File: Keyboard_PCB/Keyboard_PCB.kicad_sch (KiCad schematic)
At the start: 59 parts, among them J2 Battery, J3 JTAG, J4 EBUS, SW71 BTN, SW72 BTN, U1 STM32H7B0VBTx, U3 AP7343, U4 M95P32, Y1 25MHz, Y2 32.768 KHz

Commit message: Cleaned up project
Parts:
- removed C15, C16: 1u, Capacitor_SMD:C_0603_1608Metric, symbol Device:C_Small
- removed C21, C22: 2u2, Capacitor_SMD:C_0603_1608Metric, symbol Device:C_Small
- removed C27: 100n, Capacitor_SMD:C_0603_1608Metric, symbol Device:C_Small
- removed C9: 4u7, Capacitor_SMD:C_0603_1608Metric, symbol Device:C_Small
- removed D69: BAT54C, Package_TO_SOT_SMD:SOT-23, symbol Diode:BAT54C
- removed D72: CHARGING, LED_SMD:LED_0603_1608Metric, symbol Device:LED
- removed D73: CHARGED, LED_SMD:LED_0603_1608Metric, symbol Device:LED
- removed H1, H2, H3, H4, H5, H6: MountingHole_Pad, MountingHole:MountingHole_2.2mm_M2_DIN965_Pad, symbol Mechanical:MountingHole_Pad
- removed J2: Battery, Connector_PinHeader_2.00mm:PinHeader_1x02_P2.00mm_Vertical, symbol Connector_Generic:Conn_02x01
- removed J4: EBUS, Connector_PinHeader_2.00mm:PinHeader_2x04_P2.00mm_Vertical, symbol Connector_Generic:Conn_02x04_Counter_Clockwise
- removed JP1: Battery_EN, Jumper:SolderJumper-2_P1.3mm_Open_TrianglePad1.0x1.5mm, symbol Jumper:SolderJumper_2_Open
- removed R17: 47, Resistor_SMD:R_0603_1608Metric, symbol Device:R_Small
- removed R22: 2k2, Resistor_SMD:R_0603_1608Metric, symbol Device:R_Small
- removed R23: (1200 / batt_mAh) K ohm, Resistor_SMD:R_0603_1608Metric, symbol Device:R_Small
- removed R24, R25: 1k, Resistor_SMD:R_0603_1608Metric, symbol Device:R_Small
- removed TP1, TP2, TP3, TP4, TP5, TP6: TestPoint, TestPoint:TestPoint_THTPad_D2.0mm_Drill1.0mm, symbol Connector:TestPoint
- removed U1: STM32H7B0VBTx, Package_QFP:LQFP-100_14x14mm_P0.5mm, symbol MCU_ST_STM32H7:STM32H7B0VBTx
- removed U3: AP7343, Custom:SOT-25, symbol Marijn:AP7343
- removed U4: M95P32, Package_SO:PowerIntegrations_SO-8, symbol Marijn:M95P32
- removed U6: ~, Package_SO:MSOP-8_3x3mm_P0.65mm, symbol Marijn:TP4056
- added U1: STM32F412CGUx, Package_DFN_QFN:QFN-48-1EP_7x7mm_P0.5mm_EP5.6x5.6mm, symbol MCU_ST_STM32F4:STM32F412CGUx
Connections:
- new net: U1.23 (VSS), U1.35 (VSS), U1.47 (VSS), U1.49 (VSS)
- no-connect marks 30 -> 0
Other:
- removed sheet Grid
- removed sheet LCD
- note added: "STM32F412"
- note removed: "Battery Charging"
- note removed: "EEPROM"
- note removed: "Expansion BUS: 1. connection detection pin 1p 2. power 2p 3. tx only uart for keypresses 1p 4. SPI bus 4p TODO: bus takes up almost whole width of pcb topside"
- note removed: "IO"
- note removed: "LCD"
- note removed: "Mounting"
- note removed: "STM32H7B0vbt6"
- note removed: "VBAT"
- moved on the sheet: C1, C2, C28, C3, C4, C5, C6, C7, D70, D71, J3, L1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

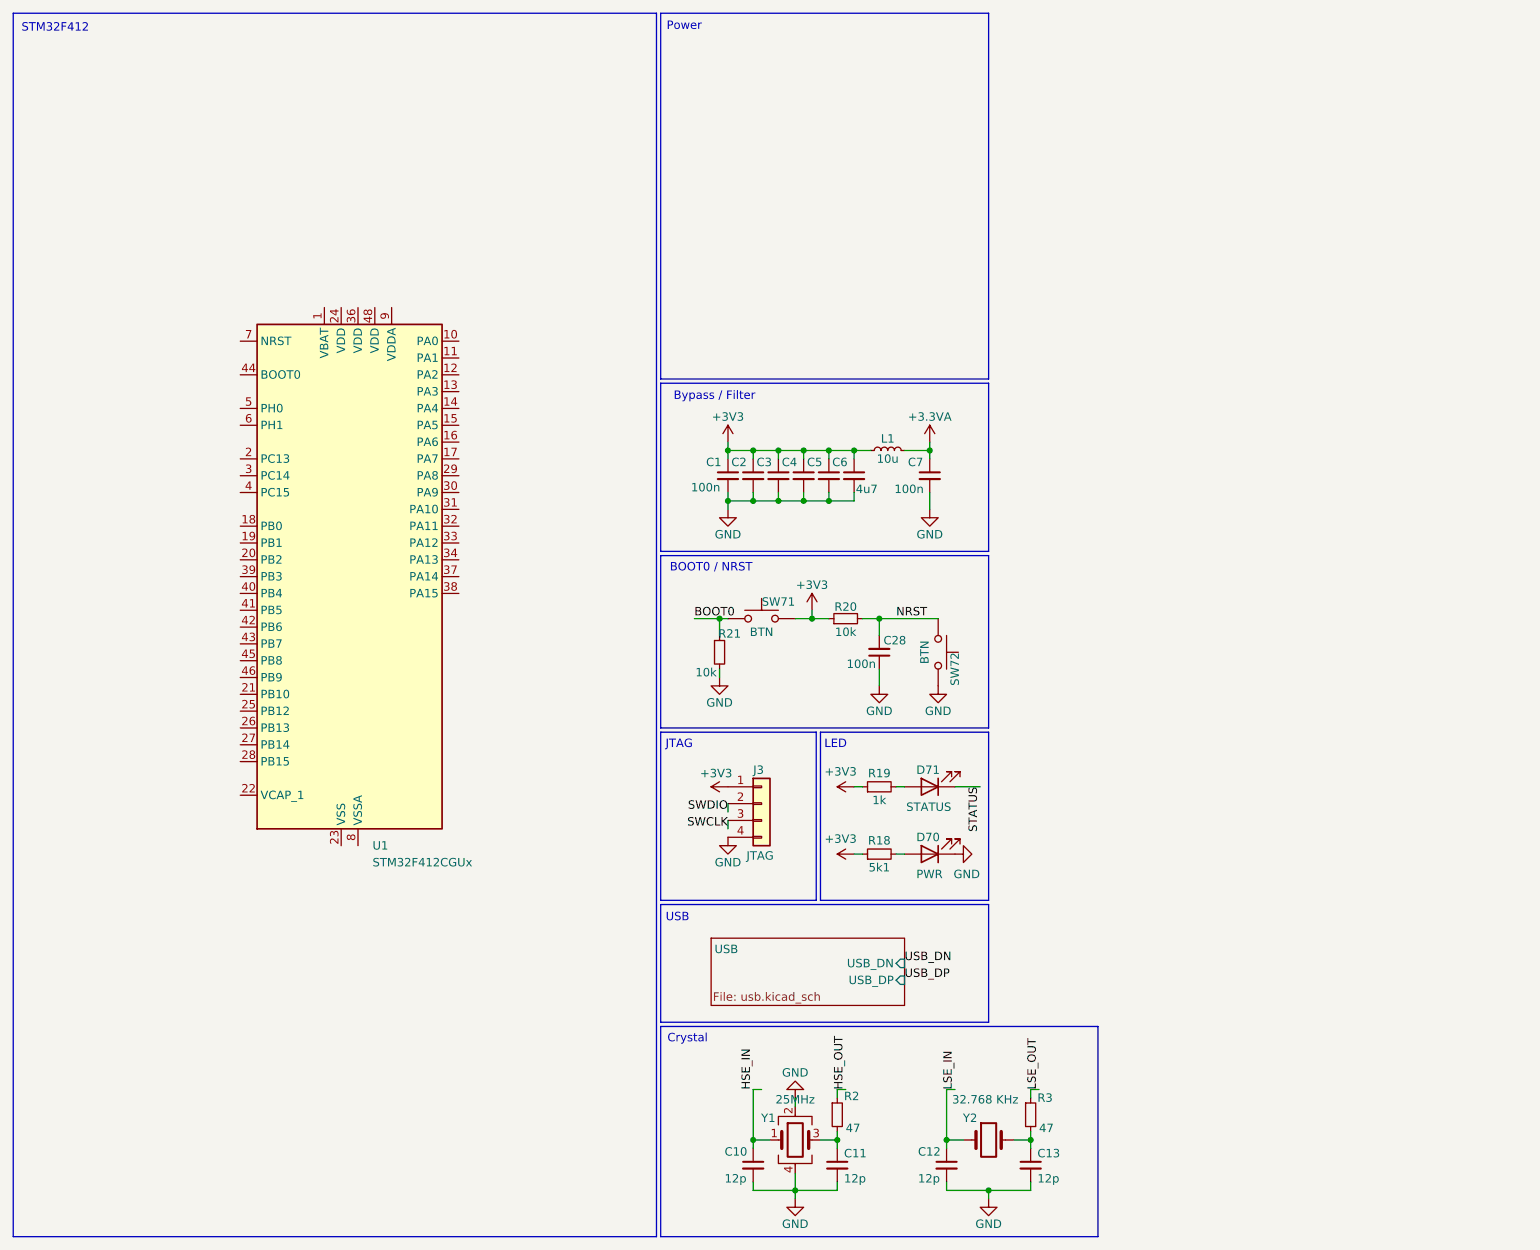
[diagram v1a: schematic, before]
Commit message: Added STM32F412
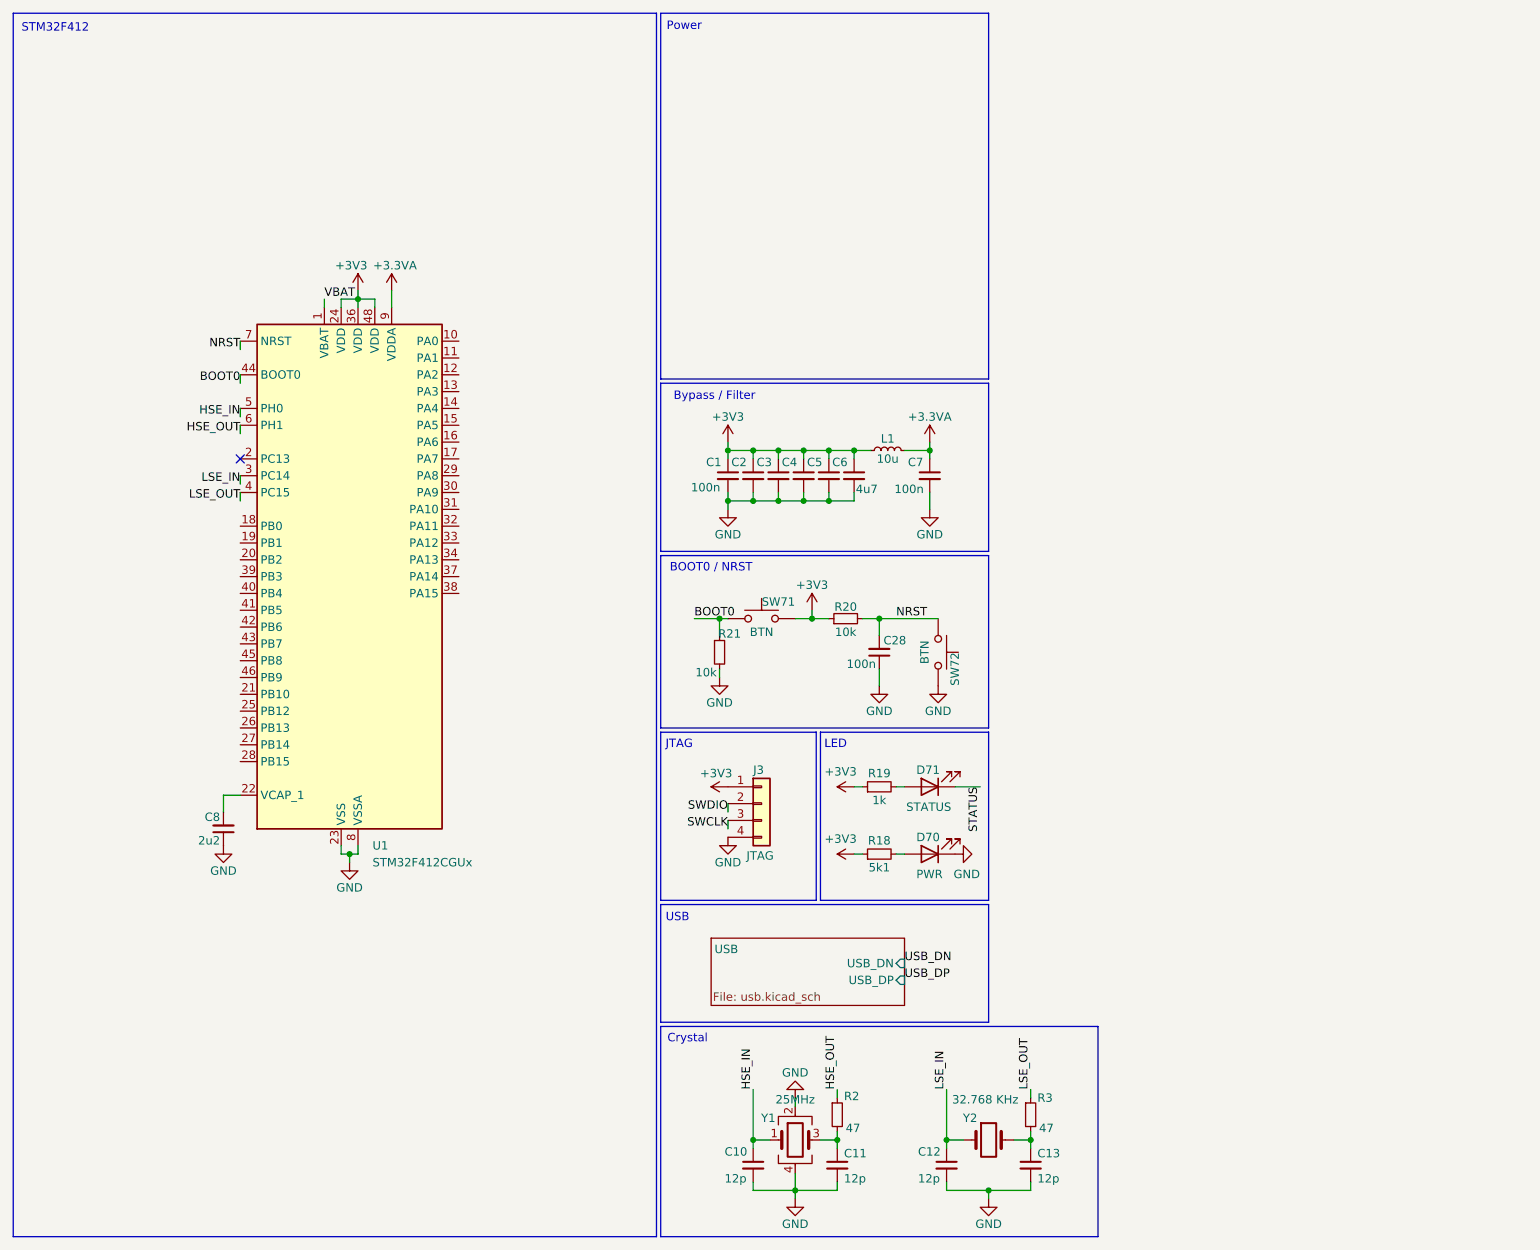
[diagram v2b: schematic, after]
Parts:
- added C8: 2u2, Capacitor_SMD:C_0603_1608Metric, symbol Device:C_Small
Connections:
- net +3.3VA: now also U1.9 (VDDA)
- net +3V3: now also U1.24 (VDD), U1.36 (VDD), U1.48 (VDD)
- net BOOT0: now also U1.44 (BOOT0)
- net GND: now also U1.23 (VSS), U1.35 (VSS), U1.47 (VSS), U1.49 (VSS), U1.8 (VSSA), C8.1
- net HSE_IN: now also U1.5 (PH0)
- net HSE_OUT: now also U1.6 (PH1)
- net LSE_IN: now also U1.3 (PC14)
- net LSE_OUT: now also U1.4 (PC15)
- net NRST: now also U1.7 (NRST)
- net VBAT: now reaches U1.1 (VBAT)
- net at U1.22 (VCAP_1): now also C8.2
- no-connect marks 0 -> 1

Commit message: Power section progress
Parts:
- renumbered C28 to C8, C8 to C9, D71 to D1, D70 to D2, J3 to J1, R20 to R1, R21 to R2, R19 to R3, R18 to R4, R2 to R5, R3 to R6, SW71 to SW1, SW72 to SW2
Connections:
- no-connect marks 1 -> 2
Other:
- sheet USB renamed USB_PWR
- sheet USB_PWR: file usb.kicad_sch -> usb_pwr.kicad_sch
- sheet USB_PWR ports: added USB_SENS, VBAT; removed none
- note added: "USB / power"
- note removed: "Power"
- note removed: "USB"
- moved on the sheet: C1, C2, C3, C4, C5, C6, C7, C8, D1, D2, J1, L1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

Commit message: Power section finished
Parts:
- added SW3: RotaryEncoder_Switch_MP, Rotary_Encoder:RotaryEncoder_Alps_EC11E-Switch_Vertical_H20mm, symbol Device:RotaryEncoder_Switch_MP
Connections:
- no-connect marks 2 -> 1
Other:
- sheet USB_PWR ports: added APP_FS, BKUP_FS; removed none
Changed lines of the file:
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@@
 		(at 46.99 80.01)
 	)
-	(no_connect
-		(at 147.32 31.75)
-	)
 	(wire
 		(pts
@@
 	(wire
 		(pts
-			(xy 147.32 30.48) (xy 147.32 29.21)
+			(xy 148.59 30.48) (xy 148.59 29.21)
 		)
 		(stroke
@@
 	(wire
 		(pts
+			(xy 119.38 29.21) (xy 119.38 27.94)
+		)
+		(stroke
+			(width 0)
+			(type default)
+		)
+	)
+	(wire
+		(pts
 			(xy 160.02 190.5) (xy 166.37 190.5)
 		)
@@
 	(wire
 		(pts
-			(xy 147.32 27.94) (xy 147.32 26.67)
+			(xy 148.59 27.94) (xy 148.59 26.67)
 		)
 		(stroke
@@
 	(wire
 		(pts
-			(xy 147.32 22.86) (xy 147.32 21.59)
+			(xy 148.59 22.86) (xy 148.59 21.59)
 		)
 		(stroke
@@
 	(wire
 		(pts
+			(xy 119.38 26.67) (xy 119.38 25.4)
+		)
+		(stroke
+			(width 0)
+			(type default)
+		)
+	)
+	(wire
+		(pts
+			(xy 148.59 33.02) (xy 148.59 31.75)
+		)
+		(stroke
+			(width 0)
+			(type default)
+		)
+	)
+	(wire
+		(pts
 			(xy 135.89 52.07) (xy 135.89 53.34)
 		)
@@
 		)
 	)
+	(label "USB_SENS"
+		(at 148.59 33.02 0)
+		(fields_autoplaced yes)
+		(effects
+			(font
+				(size 1.27 1.27)
+			)
+			(justify left bottom)
+		)
+	)
 	(label "USB_DP"
-		(at 147.32 30.48 0)
+		(at 148.59 30.48 0)
 		(fields_autoplaced yes)
 		(effects
@@
 	)
 	(label "VBAT"
-		(at 147.32 22.86 0)
+		(at 148.59 22.86 0)
 		(fields_autoplaced yes)
 		(effects
@@
 		)
 	)
+	(label "BKUP_FS"
+		(at 119.38 29.21 180)
+		(fields_autoplaced yes)
+		(effects
+			(font
+				(size 1.27 1.27)
+			)
+			(justify right bottom)
+		)
+	)
 	(label "LSE_OUT"
 		(at 166.37 175.26 90)
@@
 		)
 	)
+	(label "APP_FS"
+		(at 119.38 26.67 180)
+		(fields_autoplaced yes)
+		(effects
+			(font
+				(size 1.27 1.27)
+			)
+			(justify right bottom)
+		)
+	)
 	(label "SWDIO"
 		(at 120.65 106.68 180)
@@
 	)
 	(label "USB_DN"
-		(at 147.32 27.94 0)
+		(at 148.59 27.94 0)
 		(fields_autoplaced yes)
 		(effects
@@
 		(on_board yes)
 		(dnp no)
-		(property "Reference" "#PWR01"
+		(property "Reference" "#PWR03"
 			(at 64.77 58.42 0)
 			(effects
@@
 			(project "Keyboard_PCB"
 				(path "/dd51e792-c76c-4d43-96de-494177f3b593"
-					(reference "#PWR01")
+					(reference "#PWR03")
 					(unit 1)
 				)
@@
 		(on_board yes)
 		(dnp no)
-		(property "Reference" "#PWR04"
+		(property "Reference" "#PWR02"
 			(at 151.13 54.61 0)
 			(effects
@@
 			(project "Keyboard_PCB"
 				(path "/dd51e792-c76c-4d43-96de-494177f3b593"
-					(reference "#PWR04")
+					(reference "#PWR02")
 					(unit 1)
 				)
@@
 		(on_board yes)
 		(dnp no)
-		(property "Reference" "#PWR015"
+		(property "Reference" "#PWR014"
 			(at 143.51 113.03 0)
 			(effects
@@
 			(project "Keyboard_PCB"
 				(path "/dd51e792-c76c-4d43-96de-494177f3b593"
-					(reference "#PWR015")
+					(reference "#PWR014")
 					(unit 1)
 				)
@@
 		(on_board yes)
 		(dnp no)
-		(property "Reference" "#PWR02"
+		(property "Reference" "#PWR04"
 			(at 69.85 58.42 0)
 			(effects
@@
 			(project "Keyboard_PCB"
 				(path "/dd51e792-c76c-4d43-96de-494177f3b593"
-					(reference "#PWR02")
+					(reference "#PWR04")
 					(unit 1)
 				)
@@
 		(on_board yes)
 		(dnp no)
-		(property "Reference" "#PWR014"
+		(property "Reference" "#PWR016"
 			(at 44.45 144.78 0)
 			(effects
@@
 			(project "Keyboard_PCB"
 				(path "/dd51e792-c76c-4d43-96de-494177f3b593"
-					(reference "#PWR014")
+					(reference "#PWR016")
 					(unit 1)
 				)
@@
 	)
 	(symbol
+		(lib_id "Device:RotaryEncoder_Switch_MP")
+		(at 143.51 146.05 0)
+		(unit 1)
+		(exclude_from_sim no)
+		(in_bom yes)
+		(on_board yes)
+		(dnp no)
+		(fields_autoplaced yes)
+		(property "Reference" "SW3"
+			(at 143.51 135.89 0)
+			(effects
+				(font
+					(size 1.27 1.27)
+				)
+			)
+		)
+		(property "Value" "RotaryEncoder_Switch_MP"
+			(at 143.51 138.43 0)
+			(effects
+				(font
+					(size 1.27 1.27)
+				)
+			)
+		)
+		(property "Footprint" "Rotary_Encoder:RotaryEncoder_Alps_EC11E-Switch_Vertical_H20mm"
+			(at 139.7 141.986 0)
+			(effects
+				(font
+					(size 1.27 1.27)
+				)
+				(hide yes)
+			)
+		)
+		(property "Datasheet" "~"
+			(at 143.51 158.75 0)
+			(effects
+				(font
+					(size 1.27 1.27)
+				)
+				(hide yes)
+			)
+		)
+		(property "Description" "Rotary encoder, dual channel, incremental quadrate outputs, with switch and MP Pin"
+			(at 143.51 161.29 0)
+			(effects
+				(font
+					(size 1.27 1.27)
+				)
+				(hide yes)
+			)
+		)
+		(pin "S1"
+		)
+		(pin "MP"
+		)
+		(pin "B"
+		)
+		(pin "C"
+		)
+		(pin "S2"
+		)
+		(pin "A"
+		)
+		(instances
+			(project ""
+				(path "/dd51e792-c76c-4d43-96de-494177f3b593"
+					(reference "SW3")
+					(unit 1)
+				)
+			)
+		)
+	)
+	(symbol
 		(lib_id "Device:L_Small")
 		(at 144.78 52.07 90)
@@
 		(on_board yes)
 		(dnp no)
-		(property "Reference" "#PWR016"
+		(property "Reference" "#PWR015"
 			(at 161.29 113.03 0)
 			(effects
@@
 			(project "Keyboard_PCB"
 				(path "/dd51e792-c76c-4d43-96de-494177f3b593"
-					(reference "#PWR016")
+					(reference "#PWR015")
 					(unit 1)
 				)
@@
 		(on_board yes)
 		(dnp no)
-		(property "Reference" "#PWR03"
+		(property "Reference" "#PWR01"
 			(at 120.65 54.61 0)
 			(effects
@@
 			(project "Keyboard_PCB"
 				(path "/dd51e792-c76c-4d43-96de-494177f3b593"
-					(reference "#PWR03")
+					(reference "#PWR01")
 					(unit 1)
 				)
@@
 	)
 	(sheet
-		(at 118.11 19.05)
+		(at 119.38 19.05)
 		(size 29.21 16.51)
 		(stroke
@@
 		)
 		(property "Sheetname" "USB_PWR"
-			(at 118.618 21.463 0)
+			(at 119.888 21.463 0)
 			(effects
 				(font
@@
 		)
 		(property "Sheetfile" "usb_pwr.kicad_sch"
-			(at 118.364 33.528 0)
+			(at 119.634 33.528 0)
 			(effects
 				(font
@@
 		)
 		(pin "USB_DN" input
-			(at 147.32 26.67 0)
+			(at 148.59 26.67 0)
 			(effects
 				(font
@@
 		)
 		(pin "USB_DP" input
-			(at 147.32 29.21 0)
+			(at 148.59 29.21 0)
 			(effects
 				(font
@@
 		)
 		(pin "VBAT" input
-			(at 147.32 21.59 0)
+			(at 148.59 21.59 0)
 			(effects
 				(font
@@
 		)
 		(pin "USB_SENS" input
-			(at 147.32 31.75 0)
+			(at 148.59 31.75 0)
 			(effects
 				(font
@@
 			)
 		)
+		(pin "APP_FS" input
+			(at 119.38 25.4 180)
+			(effects
+				(font
+					(size 1.27 1.27)
+				)
+				(justify left)
+			)
+		)
+		(pin "BKUP_FS" input
+			(at 119.38 27.94 180)
+			(effects
+				(font
+					(size 1.27 1.27)
+				)
+				(justify left)
+			)
+		)

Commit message: Progress
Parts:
- added C28, C29, C30: 10n, Capacitor_SMD:C_0603_1608Metric, symbol Device:C_Small
- added J3: LCD_MODULE, symbol Connector_Generic:Conn_01x08
- added J4: FPC 30, symbol Connector_Generic:Conn_01x30
- added J5: I2C_LCD, symbol Connector_Generic:Conn_01x04
- added JP1: PWR_LED, symbol Jumper:SolderJumper_2_Open
- added R22, R23, R24, R25, R26: 10k, Resistor_SMD:R_0603_1608Metric, symbol Device:R_Small
- added U7: W25Q128JVS, Marijn_KiCad:SOIC-8_W25QxJVS, symbol Memory_Flash:W25Q128JVS
- SW3: value RotaryEncoder_Switch_MP -> EC11E15244G1
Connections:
- net +3V3: now also J3.2 (Pin_2), J3.8 (Pin_8), J5.2 (Pin_2), JP1.1 (A), R22.2, R23.2, R25.2, U7.8 (VCC); no longer R4.1
- net GND: now also SW3.C, SW3.MP, SW3.S2, C28.2, C29.2, C30.2, J3.1 (Pin_1), J5.1 (Pin_1), U7.4 (GND)
- net EC11_A: now reaches SW3.A
- net EC11_A: now also R23.1, R24.1
- net EC11_B: now reaches SW3.B
- net EC11_B: now also R25.1, R26.1
- net ENC_SW: now reaches SW3.S1
- net ENC_SW: now also C30.1, R22.1
- new net: JP1.2 (B), R4.1
- new net ENC_A: C28.1, R24.2
- new net ENC_B: C29.1, R26.2
- new net FLASH_CLK: U7.6 (CLK)
- new net FLASH_MISO: U7.2 (DO(IO1))
- new net FLASH_MOSI: U7.5 (DI(IO0))
- new net FLASH_NCS: U7.1 (~{CS})
- new net FLASH_NRST: U7.7 (IO3)
- new net FLASH_NWP: U7.3 (IO2)
- new net I2C_LCD_SCL: J5.3 (Pin_3)
- new net I2C_LCD_SDA: J5.4 (Pin_4)
- new net LCD_CLK: J3.3 (Pin_3)
- new net LCD_DC: J3.6 (Pin_6)
- new net LCD_MOSI: J3.4 (Pin_4)
- new net LCD_NCS: J3.7 (Pin_7)
- new net LCD_NRST: J3.5 (Pin_5)
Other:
- note added: "Encoder"
- note added: "I2C LCD (failsafe)"
- note added: "LCD custom"
- note added: "LCD module"
- note added: "SPI flash"
- note added: "TODO"
- moved on the sheet: D1, D2, J1, R3, R4, SW3
